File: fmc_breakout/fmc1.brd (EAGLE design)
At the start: 100 x 80 mm, 1 part

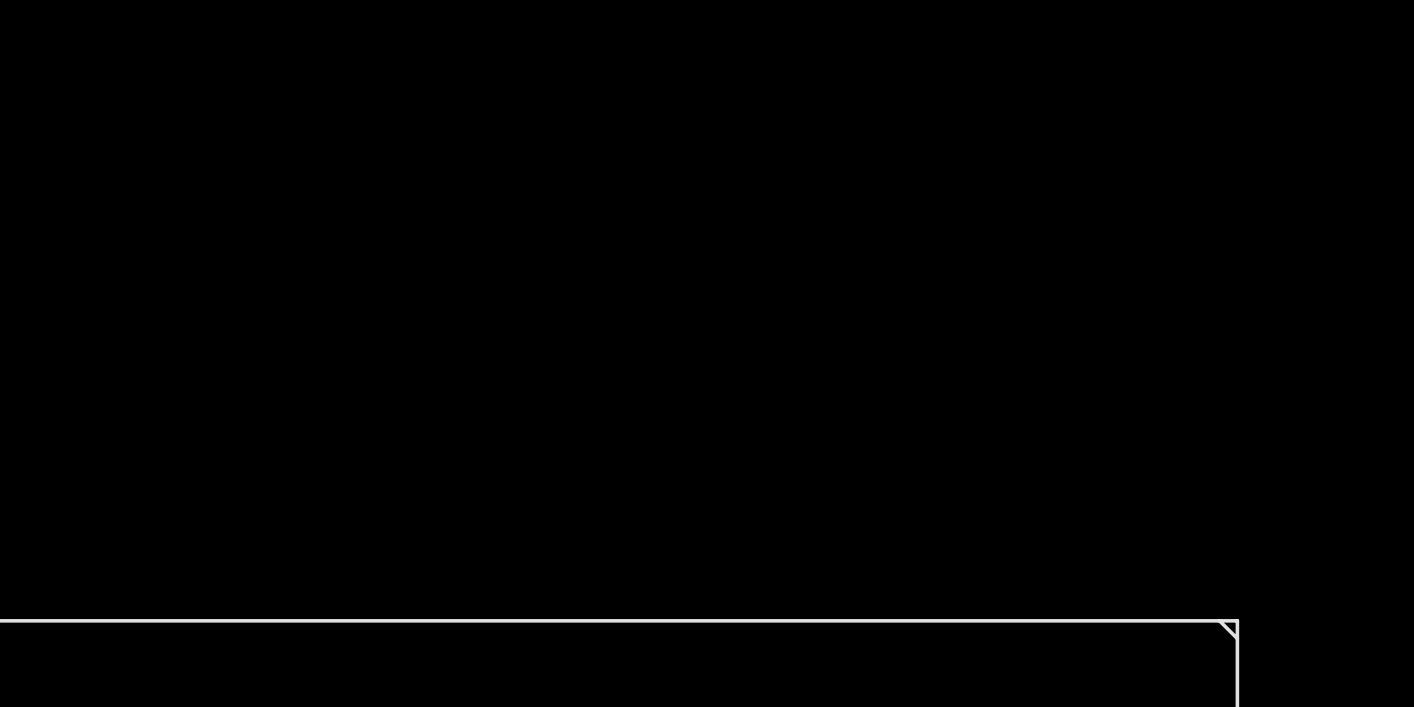
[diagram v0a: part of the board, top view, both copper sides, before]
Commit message: fixed EAGLE problems, added FIFOs to FMC breakout
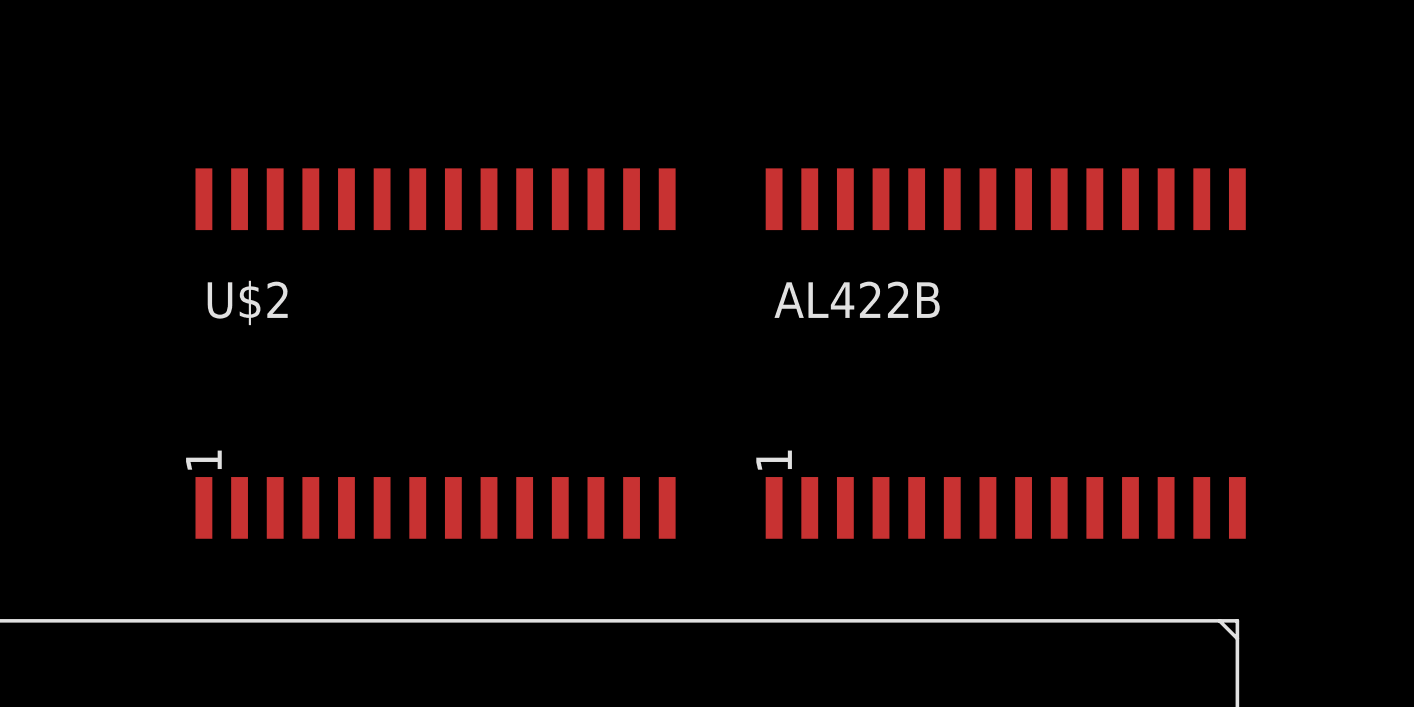
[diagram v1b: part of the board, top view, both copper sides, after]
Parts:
- added AL422B, U$2: AL422B, AL422B:SOP28
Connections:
- net LA06_N renamed L22
- net LA06_P renamed L21
- net LA10_N renamed T19
- net LA10_P renamed R19
- net LA14_N renamed K20
- net LA14_P renamed K19
- net LA18_N renamed C20
- net LA18_P renamed D20
- net LA27_N renamed D21
- net LA27_P renamed E21
- net SCL renamed SCL(R7)
- net SDA renamed SDA(U7)
- new net A16: ZED1.H31
- new net A17: ZED1.H32
- new net A18: ZED1.H28
- new net A19: ZED1.H29
- new net A21: ZED1.H37
- new net A22: ZED1.H38
- new net B15: ZED1.H35
- new net B16: ZED1.G33
- new net B17: ZED1.G34
- new net B19: ZED1.D20
- new net B20: ZED1.D21
- new net B21: ZED1.G36
- new net B22: ZED1.G37
- new net C15: ZED1.H34
- new net C17: ZED1.G30
- new net C18: ZED1.G31
- new net C22: ZED1.G28
- new net CLK0_N(L19): ZED1.H5
- new net CLK0_P(L18): ZED1.H4
- new net CLK1_N(C19): ZED1.G3
- new net CLK1_P(D18): ZED1.G2
- new net D15: ZED1.D24
- new net D22: ZED1.G27
- new net E15: ZED1.D23
- new net E18: ZED1.D27
- new net E19: ZED1.H25
- new net E20: ZED1.H26
- new net F18: ZED1.D26
- new net F19: ZED1.G25
- new net FMC-PRSNT(AB14): ZED1.H2
- new net FMC-VREF: ZED1.H1
- new net G15: ZED1.H22
- new net G16: ZED1.H23
- new net G19: ZED1.G24
- new net G20: ZED1.G21
- new net G21: ZED1.G22
- new net GA1: ZED1.D35
- new net GBTCLK0-M2C_N: ZED1.D5
- new net GBTCLK0-M2C_P: ZED1.D4
- new net GND1: AL422B.6, U$2.6
- new net GND2: AL422B.23, U$2.23
- new net J16: ZED1.H19
- new net J17: ZED1.H20
- new net J18: ZED1.D11
- new net J20: ZED1.G18
- new net J21: ZED1.G12
- new net J22: ZED1.G13
- new net K18: ZED1.D12
- new net K21: ZED1.G19
- new net L17: ZED1.D17
- new net M17: ZED1.D18
- new net M19: ZED1.G6
- new net M20: ZED1.G7
- new net M21: ZED1.H10
- new net M22: ZED1.H11
- new net N17: ZED1.H16
- new net N18: ZED1.H17
- new net N19: ZED1.D8
- new net N20: ZED1.D9
- new net N22: ZED1.G9
- new net P17: ZED1.H7
- new net P18: ZED1.H8
- new net P20: ZED1.G15
- new net P21: ZED1.G16
- new net P22: ZED1.G10
- new net PS-POR-B: ZED1.D1
- new net R20: ZED1.D14
- new net R21: ZED1.D15
- new net SHIELD: ZED1.G40
- new net T16: ZED1.H13
- new net T17: ZED1.H14
- new net TCK: ZED1.D29
- new net TDI: ZED1.D30
- new net TDO: ZED1.D31
- new net TMS: ZED1.D33
- new net TRST_L: ZED1.D34
- new net VADJ: ZED1.G39, ZED1.H40
- net 3V3: now also AL422B.10, U$2.10, ZED1.D32, ZED1.D36, ZED1.D38, ZED1.D40
- net GND: now also ZED1.D10, ZED1.D13, ZED1.D16, ZED1.D19, ZED1.D2, ZED1.D22, ZED1.D25, ZED1.D28, ZED1.D3, ZED1.D37, ZED1.D39, ZED1.D6, ZED1.D7, ZED1.G1, ZED1.G11, ZED1.G14, ZED1.G17, ZED1.G20, ZED1.G23, ZED1.G26, ZED1.G29, ZED1.G32, ZED1.G35, ZED1.G38, ZED1.G4, ZED1.G5, ZED1.G8, ZED1.H12, ZED1.H15, ZED1.H18, ZED1.H21, ZED1.H24, ZED1.H27, ZED1.H3, ZED1.H30, ZED1.H33, ZED1.H36, ZED1.H39, ZED1.H6, ZED1.H9

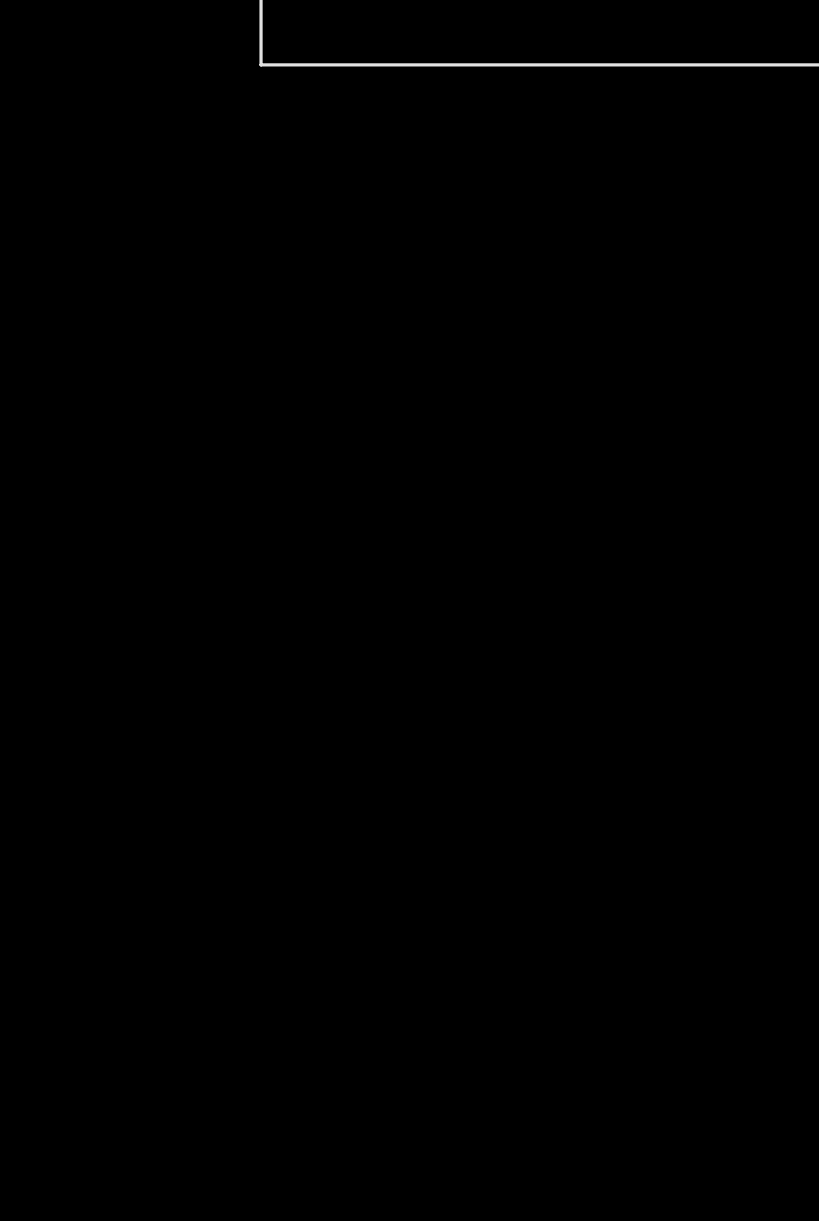
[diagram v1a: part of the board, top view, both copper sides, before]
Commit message: added camera data headers
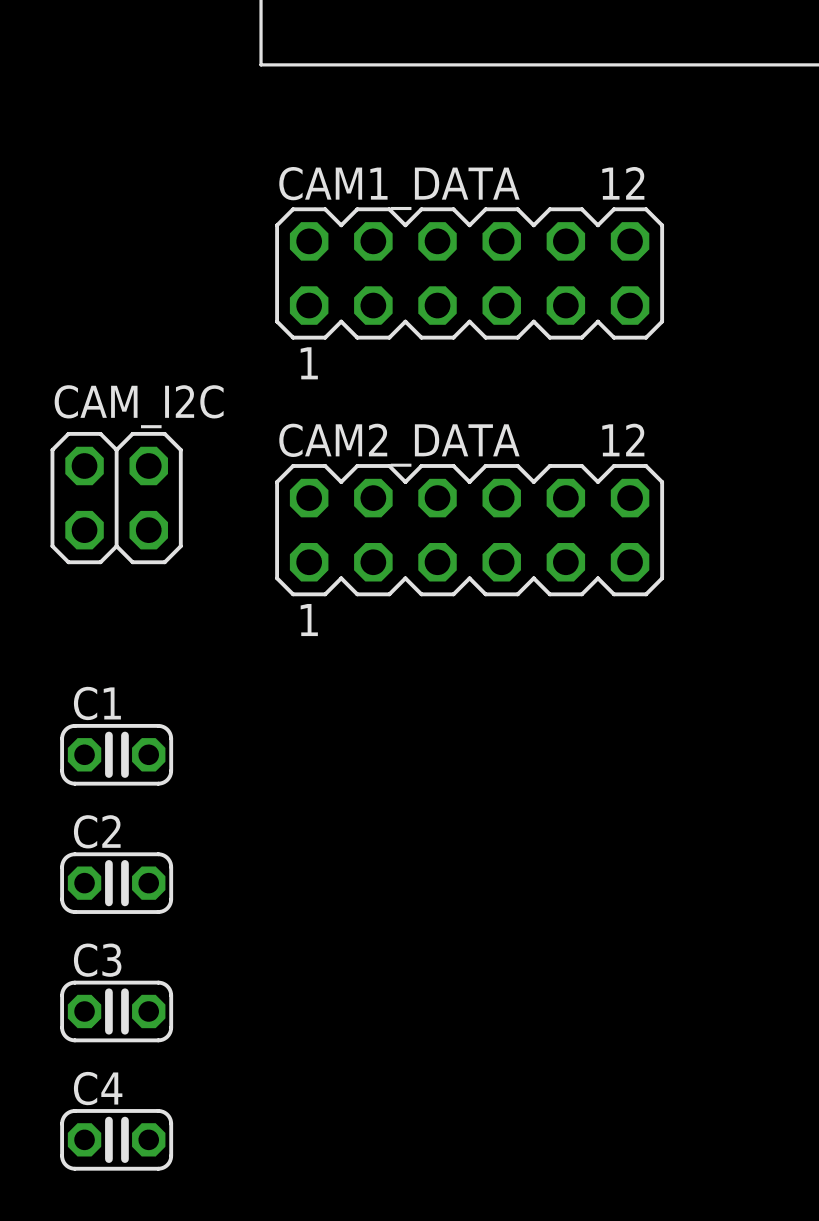
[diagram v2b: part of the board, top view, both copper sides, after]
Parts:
- added C1, C2, C3, C4: 100nf, rcl:C025-024X044
- added CAM1_DATA, CAM2_DATA: (no value), con-lstb:MA06-2
- added CAM_I2C: (no value), pinhead:2X02
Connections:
- removed net GND1: AL422B.6, U$2.6
- removed net GND2: AL422B.23, U$2.23
- new net +3V3: AL422B.19, C1.1, C2.1, U$2.19
- new net C1D2: AL422B.1, CAM1_DATA.5
- new net C1D3: AL422B.2, CAM1_DATA.6
- new net C1D4: AL422B.3, CAM1_DATA.7
- new net C1D5: AL422B.4, CAM1_DATA.8
- new net C1D6: AL422B.11, CAM1_DATA.9
- new net C1D7: AL422B.12, CAM1_DATA.10
- new net C1D8: AL422B.13, CAM1_DATA.11
- new net C1D9: AL422B.14, CAM1_DATA.12
- new net C2D2: CAM2_DATA.5, U$2.1
- new net C2D3: CAM2_DATA.6, U$2.2
- new net C2D4: CAM2_DATA.7, U$2.3
- new net C2D5: CAM2_DATA.8, U$2.4
- new net C2D6: CAM2_DATA.9, U$2.11
- new net C2D7: CAM2_DATA.10, U$2.12
- new net C2D8: CAM2_DATA.11, U$2.13
- new net C2D9: CAM2_DATA.12, U$2.14
- net 3V3: now also C3.1, C4.1
- net GND: now also AL422B.23, AL422B.24, AL422B.6, AL422B.7, C1.2, C2.2, C3.2, C4.2, U$2.23, U$2.24, U$2.6, U$2.7
- net SCL(R7): now also CAM_I2C.2, CAM_I2C.4
- net SDA(U7): now also CAM_I2C.1, CAM_I2C.3
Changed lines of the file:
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@@
 <element name="U$2" library="AL422B" package="SOP28" value="AL422B" x="-43.18" y="29.21"/>
 <element name="ZED1" library="zed-board" package="ASP-134604-01" value="ZED-BOARD" x="-43.18" y="11.43"/>
+<element name="CAM1_DATA" library="con-lstb" package="MA06-2" value="" x="-63.5" y="-5.08">
+<attribute name="OC_FARNELL" value="unknown" x="-63.5" y="-5.08" size="1.778" layer="27" display="off"/>
+<attribute name="OC_NEWARK" value="unknown" x="-63.5" y="-5.08" size="1.778" layer="27" display="off"/>
+<attribute name="MF" value="" x="-63.5" y="-5.08" size="1.778" layer="27" display="off"/>
+<attribute name="MPN" value="" x="-63.5" y="-5.08" size="1.778" layer="27" display="off"/>
+</element>
+<element name="CAM2_DATA" library="con-lstb" package="MA06-2" value="" x="-63.5" y="-15.24">
+<attribute name="OC_FARNELL" value="unknown" x="-63.5" y="-15.24" size="1.778" layer="27" display="off"/>
+<attribute name="OC_NEWARK" value="unknown" x="-63.5" y="-15.24" size="1.778" layer="27" display="off"/>
+<attribute name="MF" value="" x="-63.5" y="-15.24" size="1.778" layer="27" display="off"/>
+<attribute name="MPN" value="" x="-63.5" y="-15.24" size="1.778" layer="27" display="off"/>
+</element>
+<element name="CAM_I2C" library="pinhead" package="2X02" value="" x="-77.47" y="-13.97"/>
+<element name="C1" library="rcl" package="C025-024X044" value="100nf" x="-77.47" y="-24.13"/>
+<element name="C2" library="rcl" package="C025-024X044" value="100nf" x="-77.47" y="-29.21"/>
+<element name="C3" library="rcl" package="C025-024X044" value="100nf" x="-77.47" y="-34.29"/>
+<element name="C4" library="rcl" package="C025-024X044" value="100nf" x="-77.47" y="-39.37"/>
 </elements>
 <signals>
-<signal name="GND1">
-<contactref element="AL422B" pad="6"/>
-<contactref element="U$2" pad="6"/>
-<wire x1="-24.765" y1="23.71" x2="-45.085" y2="23.71" width="0" layer="19" extent="1-1"/>
-</signal>
-<signal name="GND2">
-<contactref element="AL422B" pad="23"/>
-<contactref element="U$2" pad="23"/>
-<wire x1="-45.085" y1="34.71" x2="-24.765" y2="34.71" width="0" layer="19" extent="1-1"/>
-</signal>
 <signal name="DP0-C2M_P">
 <contactref element="ZED1" pad="C2"/>
@@
 <contactref element="ZED1" pad="H36"/>
 <contactref element="ZED1" pad="H39"/>
+<contactref element="U$2" pad="7"/>
+<contactref element="U$2" pad="6"/>
+<contactref element="U$2" pad="23"/>
+<contactref element="AL422B" pad="7"/>
+<contactref element="AL422B" pad="23"/>
+<contactref element="AL422B" pad="6"/>
+<contactref element="U$2" pad="24"/>
+<contactref element="AL422B" pad="24"/>
+<contactref element="C1" pad="2"/>
+<contactref element="C2" pad="2"/>
+<contactref element="C3" pad="2"/>
+<contactref element="C4" pad="2"/>
+<wire x1="-76.2" y1="-34.29" x2="-76.2" y2="-39.37" width="0" layer="19" extent="1-1"/>
+<wire x1="-76.2" y1="-29.21" x2="-76.2" y2="-34.29" width="0" layer="19" extent="1-1"/>
+<wire x1="-76.2" y1="-24.13" x2="-76.2" y2="-29.21" width="0" layer="19" extent="1-1"/>
+<wire x1="-66.675" y1="8.255" x2="-76.2" y2="-24.13" width="0" layer="19" extent="1-1"/>
 <wire x1="-65.405" y1="9.525" x2="-66.675" y2="8.255" width="0" layer="19" extent="1-1"/>
 <wire x1="-62.865" y1="8.255" x2="-65.405" y2="9.525" width="0" layer="19" extent="1-1"/>
@@
 <wire x1="-19.685" y1="13.335" x2="-20.955" y2="13.335" width="0" layer="19" extent="1-1"/>
 <wire x1="-18.415" y1="14.605" x2="-19.685" y2="13.335" width="0" layer="19" extent="1-1"/>
+<wire x1="-43.815" y1="23.71" x2="-43.815" y2="14.605" width="0" layer="19" extent="1-1"/>
+<wire x1="-45.085" y1="23.71" x2="-43.815" y2="23.71" width="0" layer="19" extent="1-1"/>
+<wire x1="-23.495" y1="23.71" x2="-23.495" y2="14.605" width="0" layer="19" extent="1-1"/>
+<wire x1="-24.765" y1="23.71" x2="-23.495" y2="23.71" width="0" layer="19" extent="1-1"/>
+<wire x1="-45.085" y1="34.71" x2="-45.085" y2="23.71" width="0" layer="19" extent="1-1"/>
+<wire x1="-46.355" y1="34.71" x2="-45.085" y2="34.71" width="0" layer="19" extent="1-1"/>
+<wire x1="-24.765" y1="34.71" x2="-24.765" y2="23.71" width="0" layer="19" extent="1-1"/>
+<wire x1="-26.035" y1="34.71" x2="-24.765" y2="34.71" width="0" layer="19" extent="1-1"/>
 </signal>
 <signal name="DP0-M2C_P">
@@
 <contactref element="AL422B" pad="10"/>
 <contactref element="U$2" pad="10"/>
-<wire x1="-67.945" y1="13.335" x2="-66.675" y2="14.605" width="0" layer="19" extent="1-1"/>
+<contactref element="C3" pad="1"/>
+<contactref element="C4" pad="1"/>
+<wire x1="-78.74" y1="-34.29" x2="-78.74" y2="-39.37" width="0" layer="19" extent="1-1"/>
+<wire x1="-67.945" y1="13.335" x2="-78.74" y2="-34.29" width="0" layer="19" extent="1-1"/>
+<wire x1="-66.675" y1="14.605" x2="-67.945" y2="13.335" width="0" layer="19" extent="1-1"/>
 <wire x1="-65.405" y1="13.335" x2="-66.675" y2="14.605" width="0" layer="19" extent="1-1"/>
 <wire x1="-62.865" y1="13.335" x2="-65.405" y2="13.335" width="0" layer="19" extent="1-1"/>
@@
 <signal name="SDA(U7)">
 <contactref element="ZED1" pad="C31"/>
+<contactref element="CAM_I2C" pad="1"/>
+<contactref element="CAM_I2C" pad="3"/>
+<wire x1="-76.2" y1="-15.24" x2="-78.74" y2="-15.24" width="0" layer="19" extent="1-1"/>
+<wire x1="-56.515" y1="14.605" x2="-76.2" y2="-15.24" width="0" layer="19" extent="1-1"/>
 </signal>
 <signal name="SCL(R7)">
 <contactref element="ZED1" pad="C30"/>
+<contactref element="CAM_I2C" pad="2"/>
+<contactref element="CAM_I2C" pad="4"/>
+<wire x1="-76.2" y1="-12.7" x2="-78.74" y2="-12.7" width="0" layer="19" extent="1-1"/>
+<wire x1="-55.245" y1="14.605" x2="-76.2" y2="-12.7" width="0" layer="19" extent="1-1"/>
 </signal>
 <signal name="D21">
@@
 <wire x1="-66.675" y1="9.525" x2="-67.945" y2="8.255" width="0" layer="19" extent="1-1"/>
 </signal>
+<signal name="C1D2">
+<contactref element="CAM1_DATA" pad="5"/>
+<contactref element="AL422B" pad="1"/>
+<wire x1="-31.115" y1="23.71" x2="-64.77" y2="-6.35" width="0" layer="19" extent="1-1"/>
+</signal>
+<signal name="C1D4">
+<contactref element="CAM1_DATA" pad="7"/>
+<contactref element="AL422B" pad="3"/>
+<wire x1="-28.575" y1="23.71" x2="-62.23" y2="-6.35" width="0" layer="19" extent="1-1"/>
+</signal>
+<signal name="C1D6">
+<contactref element="CAM1_DATA" pad="9"/>
+<contactref element="AL422B" pad="11"/>
+<wire x1="-18.415" y1="23.71" x2="-59.69" y2="-6.35" width="0" layer="19" extent="1-1"/>
+</signal>
+<signal name="C1D8">
+<contactref element="CAM1_DATA" pad="11"/>
+<contactref element="AL422B" pad="13"/>
+<wire x1="-15.875" y1="23.71" x2="-57.15" y2="-6.35" width="0" layer="19" extent="1-1"/>
+</signal>
+<signal name="C1D9">
+<contactref element="CAM1_DATA" pad="12"/>
+<contactref element="AL422B" pad="14"/>
+<wire x1="-14.605" y1="23.71" x2="-57.15" y2="-3.81" width="0" layer="19" extent="1-1"/>
+</signal>
+<signal name="C1D7">
+<contactref element="CAM1_DATA" pad="10"/>
+<contactref element="AL422B" pad="12"/>
+<wire x1="-17.145" y1="23.71" x2="-59.69" y2="-3.81" width="0" layer="19" extent="1-1"/>
+</signal>
+<signal name="C1D5">
+<contactref element="CAM1_DATA" pad="8"/>
+<contactref element="AL422B" pad="4"/>
+<wire x1="-27.305" y1="23.71" x2="-62.23" y2="-3.81" width="0" layer="19" extent="1-1"/>
+</signal>
+<signal name="C1D3">
+<contactref element="CAM1_DATA" pad="6"/>
+<contactref element="AL422B" pad="2"/>
+<wire x1="-29.845" y1="23.71" x2="-64.77" y2="-3.81" width="0" layer="19" extent="1-1"/>
+</signal>
+<signal name="C2D2">
+<contactref element="U$2" pad="1"/>
+<contactref element="CAM2_DATA" pad="5"/>
+<wire x1="-51.435" y1="23.71" x2="-64.77" y2="-16.51" width="0" layer="19" extent="1-1"/>
+</signal>
+<signal name="C2D3">
+<contactref element="U$2" pad="2"/>
+<contactref element="CAM2_DATA" pad="6"/>
+<wire x1="-50.165" y1="23.71" x2="-64.77" y2="-13.97" width="0" layer="19" extent="1-1"/>
+</signal>
+<signal name="C2D4">
+<contactref element="U$2" pad="3"/>
+<contactref element="CAM2_DATA" pad="7"/>
+<wire x1="-48.895" y1="23.71" x2="-62.23" y2="-16.51" width="0" layer="19" extent="1-1"/>
+</signal>
+<signal name="C2D5">
+<contactref element="U$2" pad="4"/>
+<contactref element="CAM2_DATA" pad="8"/>
+<wire x1="-47.625" y1="23.71" x2="-62.23" y2="-13.97" width="0" layer="19" extent="1-1"/>
+</signal>
+<signal name="C2D6">
+<contactref element="U$2" pad="11"/>
+<contactref element="CAM2_DATA" pad="9"/>
+<wire x1="-38.735" y1="23.71" x2="-59.69" y2="-16.51" width="0" layer="19" extent="1-1"/>
+</signal>
+<signal name="C2D7">
+<contactref element="U$2" pad="12"/>
+<contactref element="CAM2_DATA" pad="10"/>
+<wire x1="-37.465" y1="23.71" x2="-59.69" y2="-13.97" width="0" layer="19" extent="1-1"/>
+</signal>
+<signal name="C2D8">
+<contactref element="U$2" pad="13"/>
+<contactref element="CAM2_DATA" pad="11"/>
+<wire x1="-36.195" y1="23.71" x2="-57.15" y2="-16.51" width="0" layer="19" extent="1-1"/>
+</signal>
+<signal name="C2D9">
+<contactref element="U$2" pad="14"/>
+<contactref element="CAM2_DATA" pad="12"/>
+<wire x1="-34.925" y1="23.71" x2="-57.15" y2="-13.97" width="0" layer="19" extent="1-1"/>
+</signal>
+<signal name="+3V3">
+<contactref element="AL422B" pad="19"/>
+<contactref element="U$2" pad="19"/>
+<contactref element="C1" pad="1"/>
+<contactref element="C2" pad="1"/>
+<wire x1="-78.74" y1="-24.13" x2="-78.74" y2="-29.21" width="0" layer="19" extent="1-1"/>
+<wire x1="-40.005" y1="34.71" x2="-78.74" y2="-24.13" width="0" layer="19" extent="1-1"/>
+<wire x1="-19.685" y1="34.71" x2="-40.005" y2="34.71" width="0" layer="19" extent="1-1"/>
+</signal>
 </signals>
